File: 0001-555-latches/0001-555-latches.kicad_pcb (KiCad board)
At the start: 2 copper layers, 88 x 75 mm, 37 parts, among them J1 DC_IN, J2 ASTBL_OUT, J3 BSTBL_OUT, J4 MSTBL_OUT, SW1 SW_Push, SW2 SW_Push, SW3 SW_Push, U1 NE555P, U2 NE555P, U3 NE555P

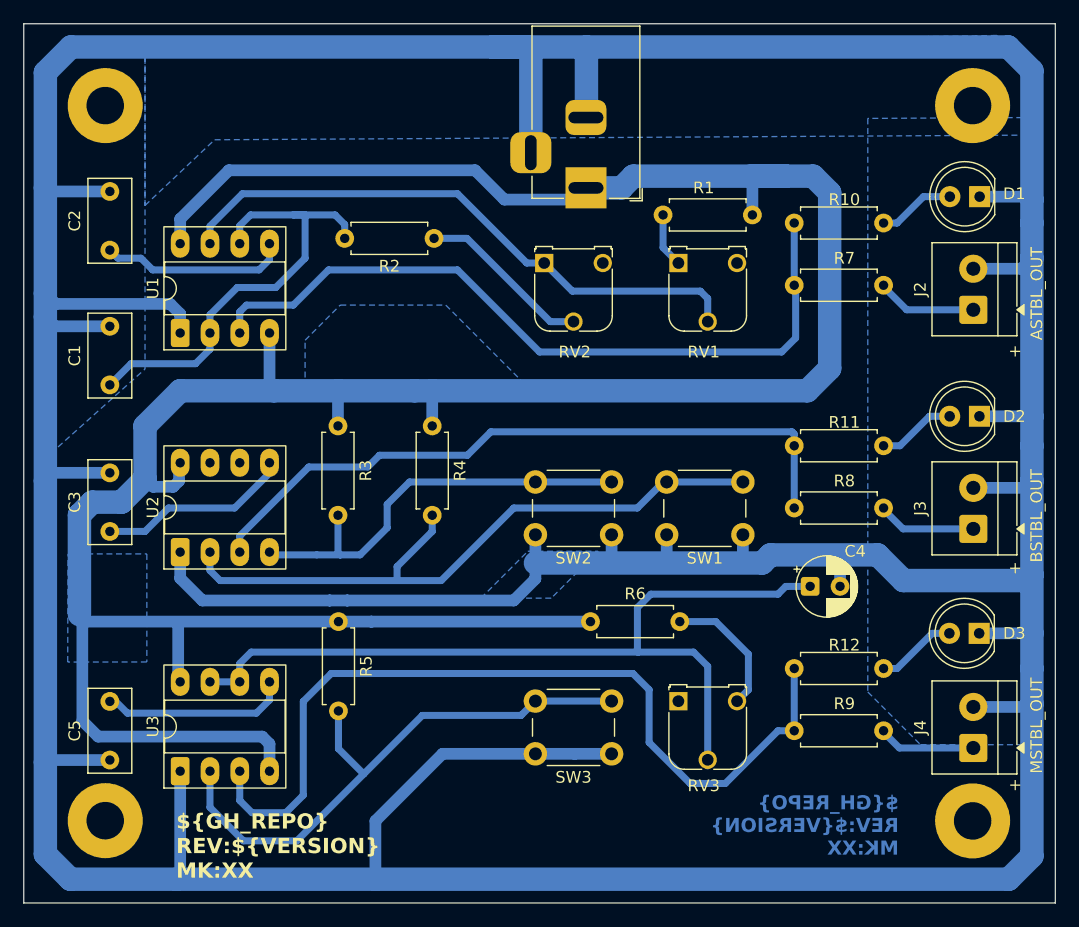
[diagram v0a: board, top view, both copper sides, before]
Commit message: Update GH organisation in PCB
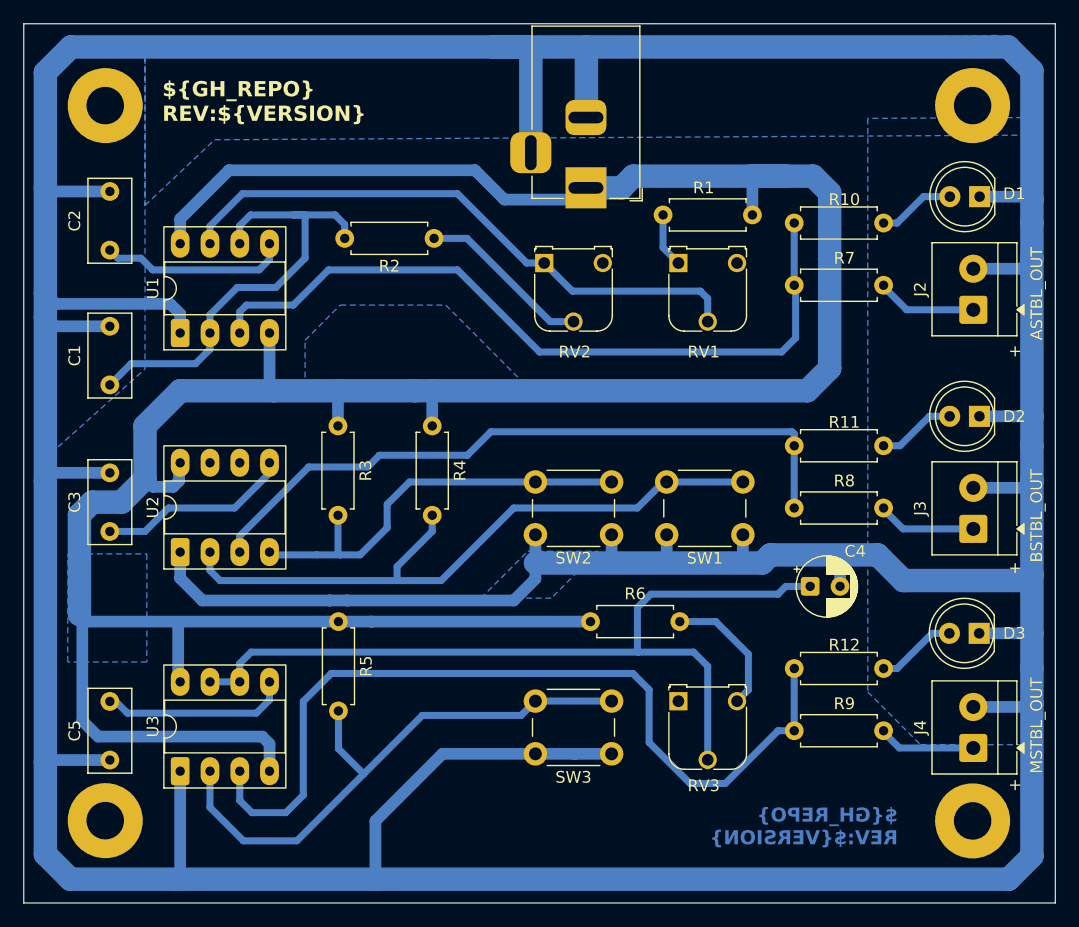
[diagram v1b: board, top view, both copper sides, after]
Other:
- board text added: "${GH_REPO} REV:${VERSION}"
- board text removed: "${GH_REPO} REV:${VERSION} MK:XX"
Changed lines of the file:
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@@
 		)
 	)
-	(property "GH_REPO" "https://github.com/marcinciapa-el/0001")
+	(property "GH_REPO" "github.com/mc-hw/0001")
 	(property "VERSION" "1.0.0")
 	(net 0 "")
@@
 		(layer "Edge.Cuts")
 	)
-	(gr_text "${GH_REPO}\nREV:${VERSION}\nMK:XX"
-		(at 175.644275 132.023504 0)
+	(gr_text "${GH_REPO}\nREV:${VERSION}"
+		(at 175.57 131.14 0)
 		(layer "B.Cu")
 		(effects
@@
 		)
 	)
-	(gr_text "${GH_REPO}\nREV:${VERSION}\nMK:XX"
-		(at 114 134 0)
+	(gr_text "${GH_REPO}\nREV:${VERSION}"
+		(at 112.813608 69.44284 0)
 		(layer "F.SilkS")
 		(effects

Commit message: Correcting files
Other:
- board text added: "${GH_REPO} Rev: ${VERSION}"
- board text removed: "${GH_REPO} REV:${VERSION}"
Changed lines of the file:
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@@
 		(layer "Edge.Cuts")
 	)
-	(gr_text "${GH_REPO}\nREV:${VERSION}"
+	(gr_text "${GH_REPO}\nRev: ${VERSION}"
 		(at 175.57 131.14 0)
 		(layer "B.Cu")
@@
 		)
 	)
-	(gr_text "${GH_REPO}\nREV:${VERSION}"
+	(gr_text "${GH_REPO}\nRev: ${VERSION}"
 		(at 112.813608 69.44284 0)
 		(layer "F.SilkS")
